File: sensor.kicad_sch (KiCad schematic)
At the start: 4 parts, among them J5 CON-SM04B-SRSS-TB, U7 LIS2DH12TR

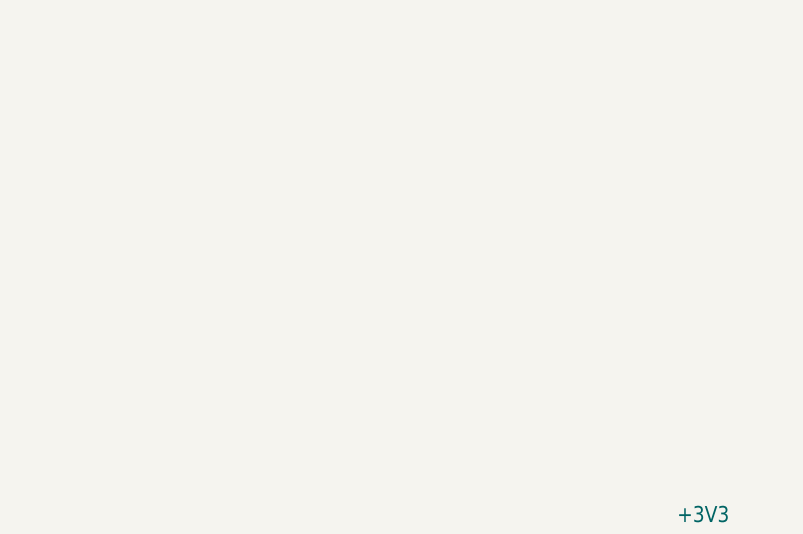
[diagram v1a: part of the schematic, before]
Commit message: v2 Changes:
1. Added STS4x to sensors
2. Relocated NTC away from nPM1300
3. Updated footprint for new USB connector
4. Optimized other footprint paste aperture
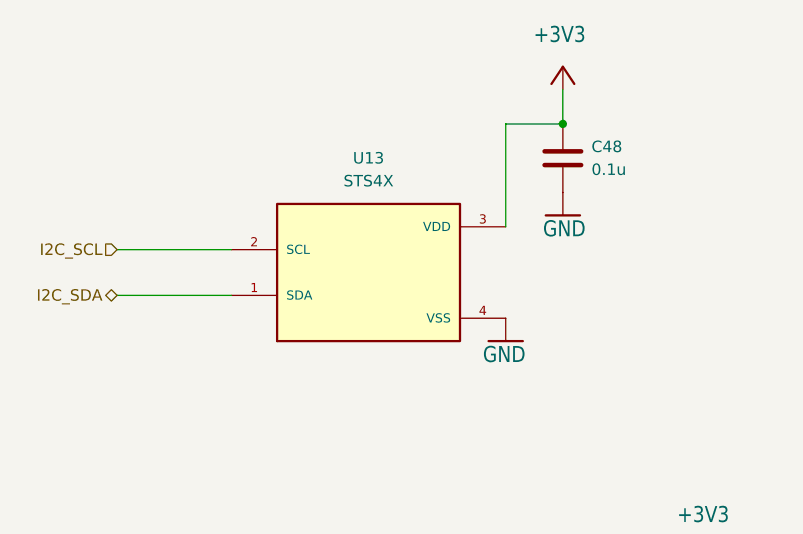
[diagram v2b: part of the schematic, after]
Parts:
- added C48: 0.1u, Capacitor_SMD:C_0402_1005Metric, symbol Device:C
- added U13: STS4X, Circuit Dojo:STS4X, symbol Circuit Dojo:STS4X
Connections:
- net +3V3: now also C48.1, U13.3 (VDD)
- net GND: now also C48.2, U13.4 (VSS)
- net I2C_SCL: now also U13.2 (SCL)
- net I2C_SDA: now also U13.1 (SDA)

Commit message: Adding variant control
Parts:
- U13: Circuit Dojo PN (none) -> IC-STS40-AD1B-R3
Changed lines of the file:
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@@
+			)
+		)
+		(property "Circuit Dojo PN" "IC-STS40-AD1B-R3"
+			(at 90.17 60.96 0)
+			(effects
+				(font
+					(size 1.27 1.27)
+				)
+				(hide yes)
 			)
 		)

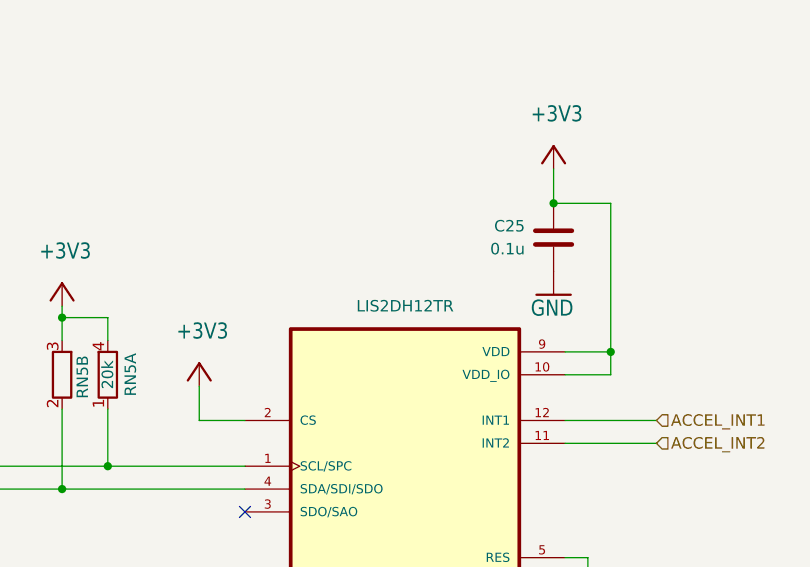
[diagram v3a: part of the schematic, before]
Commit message: PCB cleanup: reduce ground connections and set isolation to 0.2mm
- Reducing the size of ground connections
- Changing isolation to 0.2mm for all layers
- Adding border isolation 0.2mm
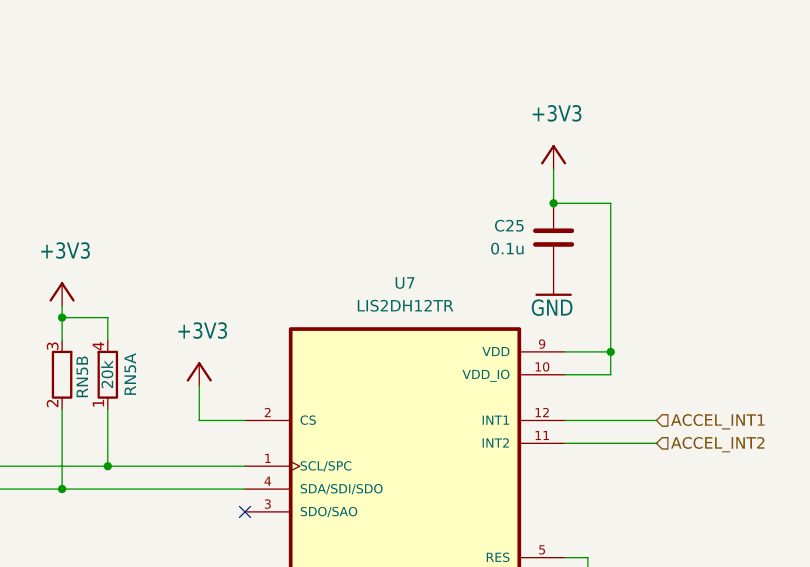
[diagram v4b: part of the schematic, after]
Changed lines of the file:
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@@
 					(size 1.27 1.27)
 				)
-				(hide yes)
 			)
 		)
